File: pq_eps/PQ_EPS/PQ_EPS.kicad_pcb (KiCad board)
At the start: 4 copper layers, 40 x 40 mm, 87 parts, among them IC1 DS2782E+, IC2 ISL9120IRTNZ, J1 CES-110-02-L-S, J2 CES-110-02-L-S, J3 CES-110-02-L-S, J4 CES-110-02-L-S, Q1 SIR424DP, U1 SPV1040TTR, U2 SPV1040TTR, U3 SPV1040TTR, U4 LTC4040EUFD#PBF

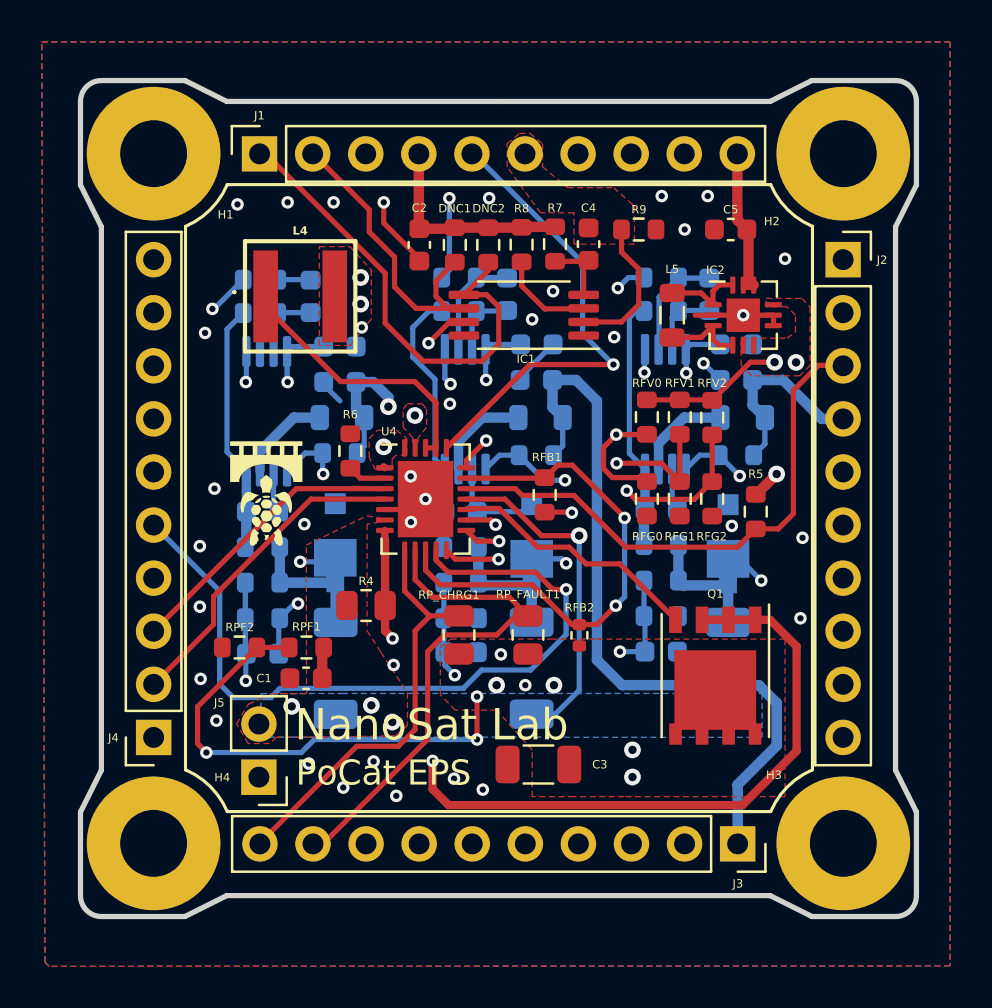
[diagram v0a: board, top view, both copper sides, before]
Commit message: small changes: change ID R5 to Rbias, add snail logo, and swap SOLARZ with GND
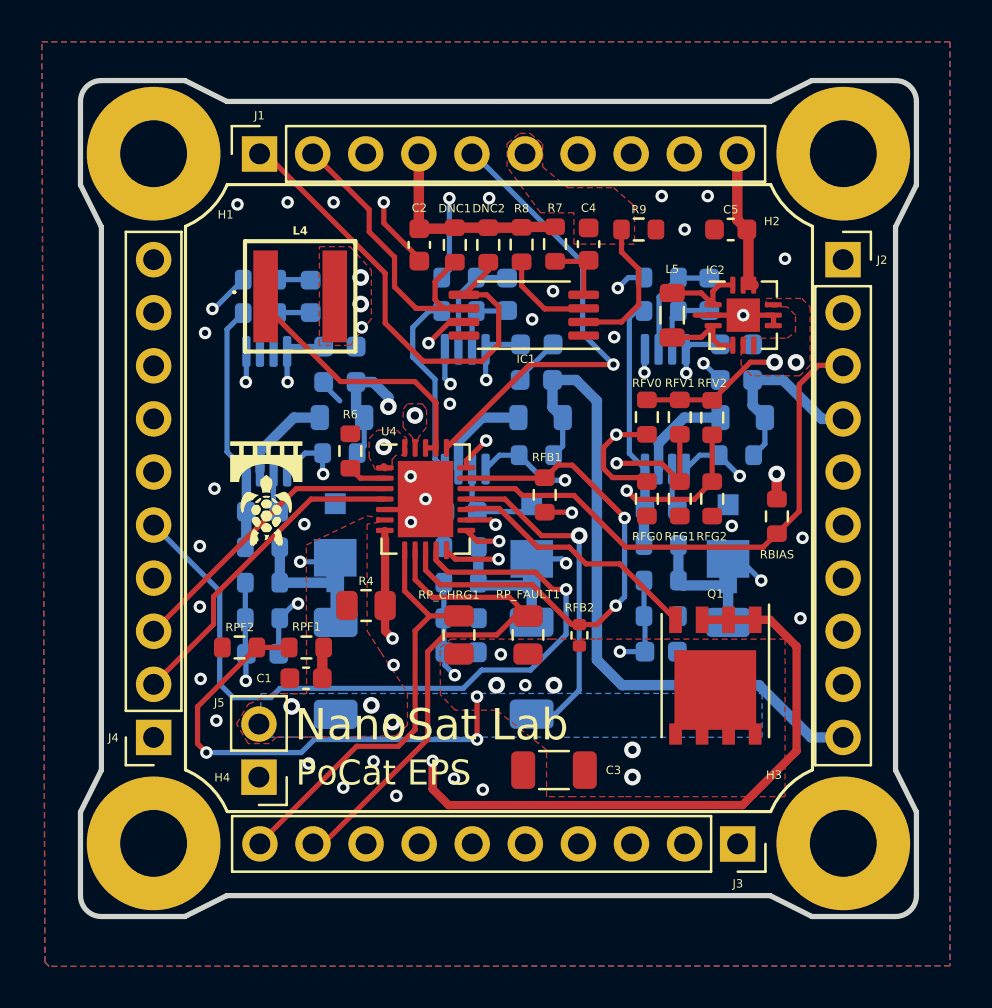
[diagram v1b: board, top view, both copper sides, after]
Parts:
- removed R5: 10k, Resistor_SMD:R_0603_1608Metric
- added Annotation3: Silkscreen_Annotation, symbols-nsl:Snail, B.Cu at (104.0, 71.7)
- added RBIAS1: 10k, Resistor_SMD:R_0603_1608Metric, F.Cu at (115.0, 58.8)
- moved C3 0.79 mm to (104.3, 71.0)
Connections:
- net TOTAL_CURRENT renamed NC
- J2 pad 10: GND -> SOLAR_Z
- J3 pad 1: SOLAR_Z -> GND
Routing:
- net SOLAR_Z: track 35.9 -> 32.2 mm
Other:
- board text added: "RBIAS"

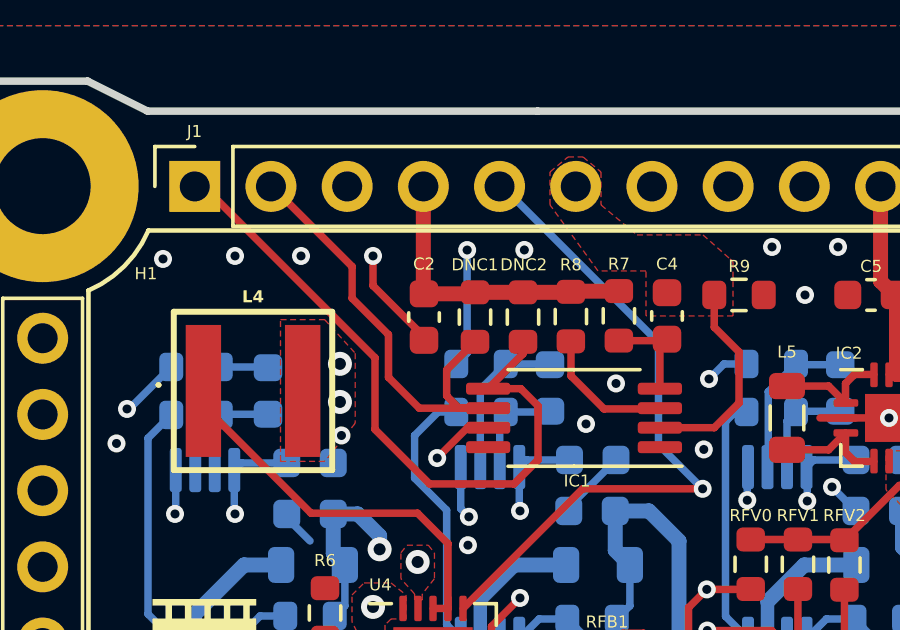
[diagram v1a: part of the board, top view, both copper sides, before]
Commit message: change RST_DRIVERS to STM32_PA9, swap SCL3 with NC, and change NC to PH_PL
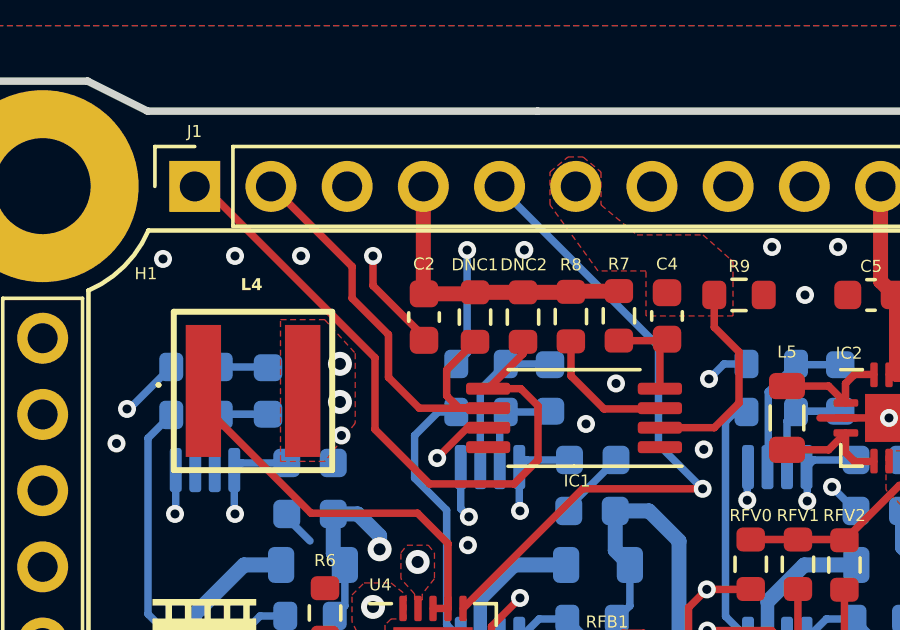
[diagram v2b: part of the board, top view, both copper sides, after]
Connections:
- net RST_DRIVERS renamed STM32_PA9
- J1 pad 7: NC -> SCL3
- J4 pad 10: SCL3 -> PH_PL
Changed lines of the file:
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@@
   (net 24 "Net-(U3-VCTRL)")
   (net 25 "unconnected-(IC1-N.C.-Pad1)")
-  (net 26 "NC")
+  (net 26 "STM32_PA9")
   (net 27 "Net-(IC1-VIN)")
   (net 28 "PFO")
@@
   (net 43 "P{slash}L_POWER")
   (net 44 "ADC_PH")
-  (net 45 "RST_DRIVERS")
+  (net 45 "PH_PL")
   (net 46 "ADCS_POWER")
   (net 47 "STM32_PB0")
@@
     (property "ki_keywords" "inductor choke coil reactor magnetic")
     (attr smd)
-    (fp_text reference "L4" (at 0 -3.1388) (layer "F.SilkS")
+    (fp_text reference "L4" (at -0.0472 -3.5452) (layer "F.SilkS")
         (effects (font (size 0.4 0.4) (thickness 0.1) bold))
     )
@@
       (net 3 "BATT-") (pinfunction "Pin_6") (pintype "passive"))
     (pad "7" thru_hole oval locked (at -0.0092 15.24 90) (size 1.7 1.7) (drill 1) (layers "*.Cu" "*.Mask")
-      (net 26 "NC") (pinfunction "Pin_7") (pintype "passive"))
+      (net 48 "SCL3") (pinfunction "Pin_7") (pintype "passive"))
     (pad "8" thru_hole oval locked (at -0.0092 17.78 90) (size 1.7 1.7) (drill 1) (layers "*.Cu" "*.Mask")
       (net 14 "UART_TX") (pinfunction "Pin_8") (pintype "passive"))
@@
       (net 49 "ADC_PL") (pinfunction "Pin_9") (pintype "passive"))
     (pad "10" thru_hole oval locked (at -0.0092 22.86 180) (size 1.7 1.7) (drill 1) (layers "*.Cu" "*.Mask")
-      (net 48 "SCL3") (pinfunction "Pin_10") (pintype "passive"))
+      (net 45 "PH_PL") (pinfunction "Pin_10") (pintype "passive"))
     (model "${KICAD_NSL_DIR}/connector-nsl/StepFiles/SLW-110-01-G-S.stp"
       (offset (xyz 0 -11.5 0))
@@
       (net 46 "ADCS_POWER") (pinfunction "Pin_3") (pintype "passive"))
     (pad "4" thru_hole oval (at -0.0092 7.62 270) (size 1.7 1.7) (drill 1) (layers "*.Cu" "*.Mask")
-      (net 45 "RST_DRIVERS") (pinfunction "Pin_4") (pintype "passive"))
+      (net 26 "STM32_PA9") (pinfunction "Pin_4") (pintype "passive"))
     (pad "5" thru_hole oval (at -0.0092 10.16 270) (size 1.7 1.7) (drill 1) (layers "*.Cu" "*.Mask")
       (net 44 "ADC_PH") (pinfunction "Pin_5") (pintype "passive"))
@@
   (segment (start 107.188 51.562) (end 103.188 51.562) (width 0.25) (layer "F.Cu") (net 28))
   (via (at 107.188 51.562) (size 0.6) (drill 0.3) (layers "F.Cu" "B.Cu") (net 28))
-  (segment (start 105.7148 46.6852) (end 100.4776 41.448) (width 0.25) (layer "B.Cu") (net 28))
   (segment (start 107.188 51.562) (end 105.7148 50.0888) (width 0.25) (layer "B.Cu") (net 28))
-  (segment (start 100.4776 41.448) (end 100.418 41.448) (width 0.25) (layer "B.Cu") (net 28))
-  (segment (start 105.7148 50.0888) (end 105.7148 46.6852) (width 0.25) (layer "B.Cu") (net 28))
+  (segment (start 105.7148 46.8114) (end 100.418 41.5146) (width 0.25) (layer "B.Cu") (net 28))
+  (segment (start 105.7148 50.0888) (end 105.7148 46.8114) (width 0.25) (layer "B.Cu") (net 28))
+  (segment (start 100.418 41.5146) (end 100.418 41.448) (width 0.25) (layer "B.Cu") (net 28))
   (segment (start 96.716 47.8464) (end 96.716 46.424) (width 0.25) (layer "F.Cu") (net 30))
   (segment (start 99.067 48.875) (end 100.0375 48.875) (width 0.25) (layer "F.Cu") (net 30))

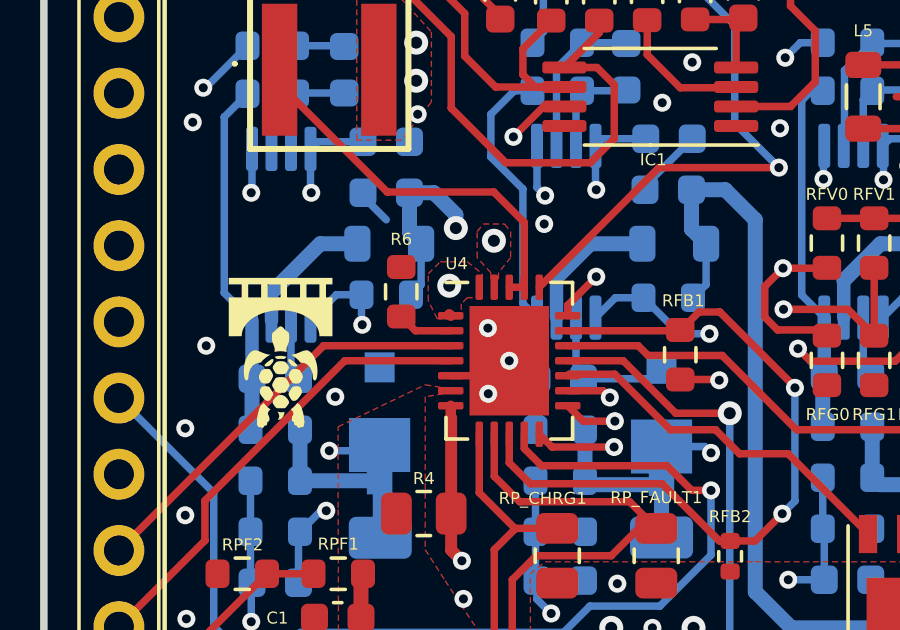
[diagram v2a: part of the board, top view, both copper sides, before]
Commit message: Cambiar etiquetas de red a etiquetas globales (Major RID 66)
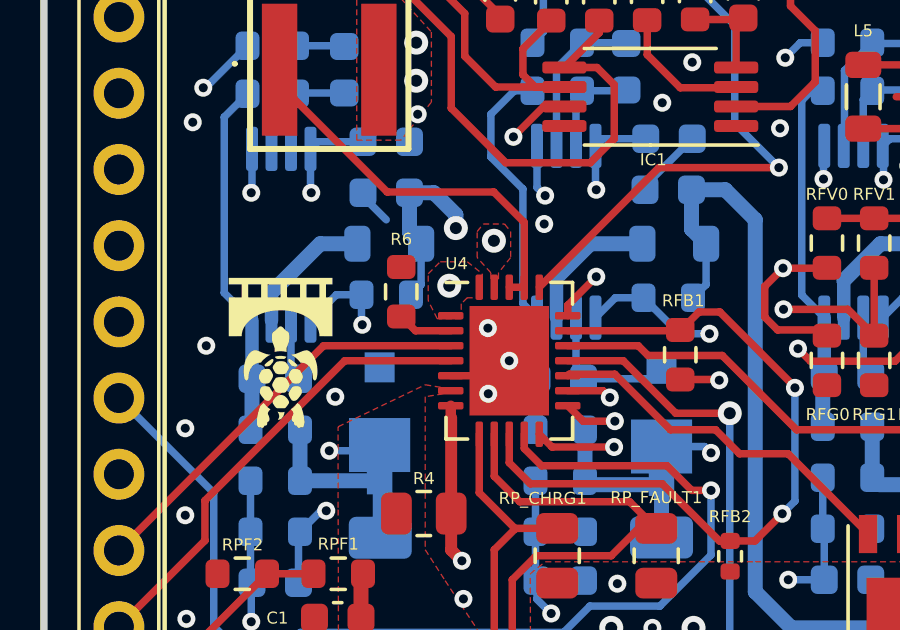
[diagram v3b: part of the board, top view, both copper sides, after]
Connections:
- net /F0 renamed F0
- net /F1 renamed F1
- net /F2 renamed F2
- net /PROG renamed PROG

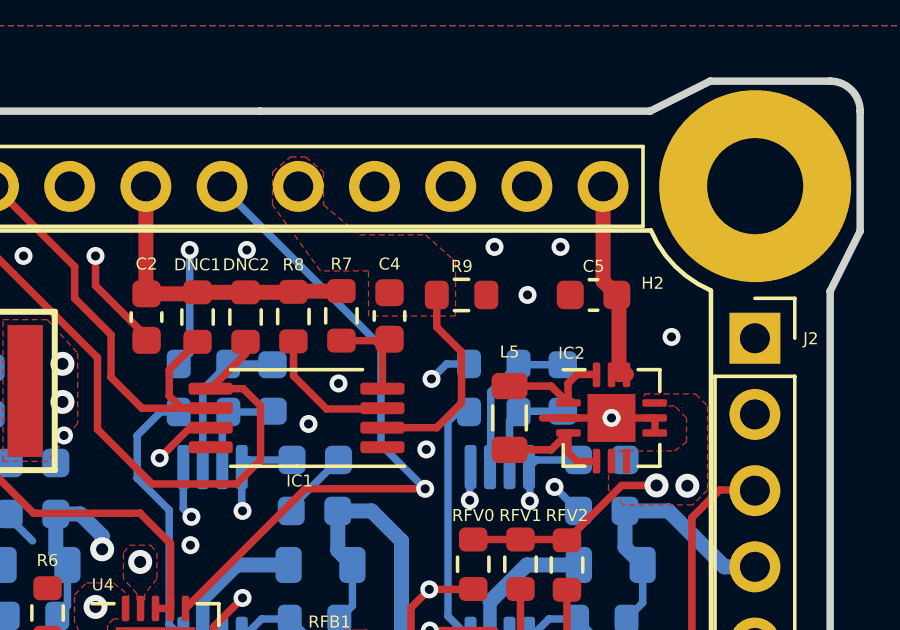
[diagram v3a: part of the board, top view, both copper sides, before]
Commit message: EPS Changes done. Voltage Regulator ENABLED by Killswitch+
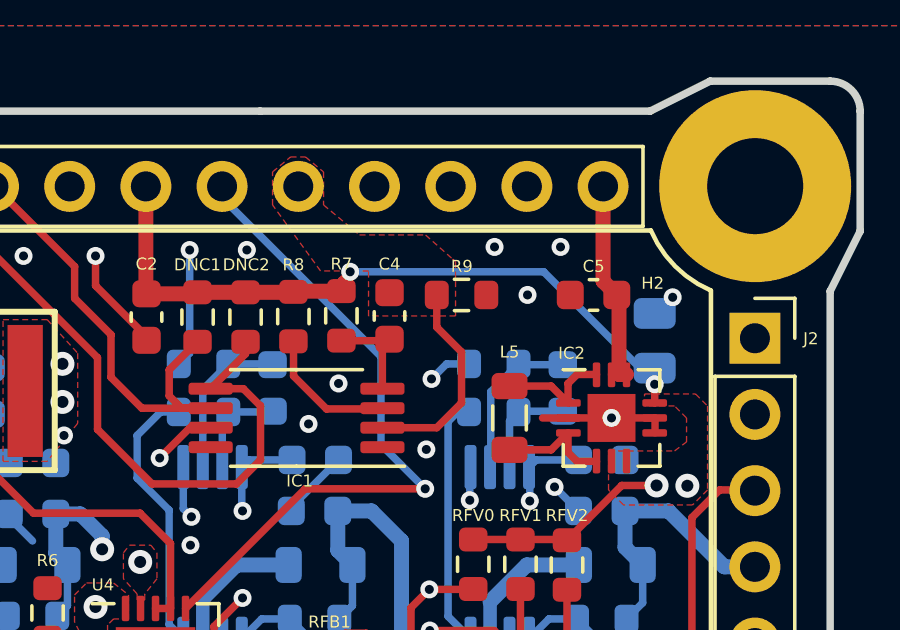
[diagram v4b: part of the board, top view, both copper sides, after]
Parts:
- added R5: 10M, Resistor_SMD:R_0805_2012Metric, B.Cu at (114.8, 46.6)
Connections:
- IC2 pad 9: CHOUT -> KILLSWITCH+
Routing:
- net KILLSWITCH+: track 10.2 -> 23.6 mm, vias 3 -> 5
